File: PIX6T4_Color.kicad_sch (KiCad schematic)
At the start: 44 parts, among them J1 USB_C_Receptacle_USB2.0_16P, J2 Conn_01x18_Pin, J8 Conn_01x03, J9 SM03B-SRSS-TB, SW1 SW_MEC_5G, SW10 SW_MEC_5G, SW11 SW_MEC_5G, SW12 SW_MEC_5G, SW2 SW_MEC_5G, SW3 SW_MEC_5G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

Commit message: Rev. 2
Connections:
- net A: now also SW7.3 (B), SW7.4 (B), U3.7 (GPIO5); no longer SW8.3 (B), SW8.4 (B), U3.9 (GPIO7)
- net B: now also SW8.3 (B), SW8.4 (B), U3.9 (GPIO7); no longer SW7.3 (B), SW7.4 (B), U3.7 (GPIO5)
- net RGB63/RGB_OUT renamed RGB71/RGB_OUT
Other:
- added sheet RGB64 (RGB.kicad_sch)
- added sheet RGB65 (RGB.kicad_sch)
- added sheet RGB66 (RGB.kicad_sch)
- added sheet RGB67 (RGB.kicad_sch)
- added sheet RGB68 (RGB.kicad_sch)
- added sheet RGB69 (RGB.kicad_sch)
- added sheet RGB70 (RGB.kicad_sch)
- added sheet RGB71 (RGB.kicad_sch)
- moved on the sheet: J8

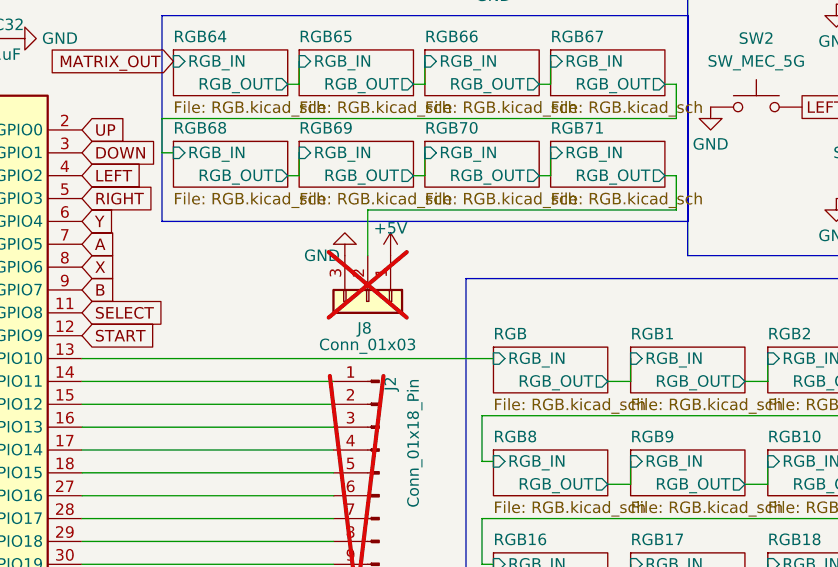
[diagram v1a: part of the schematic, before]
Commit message: Add power / invader logo light
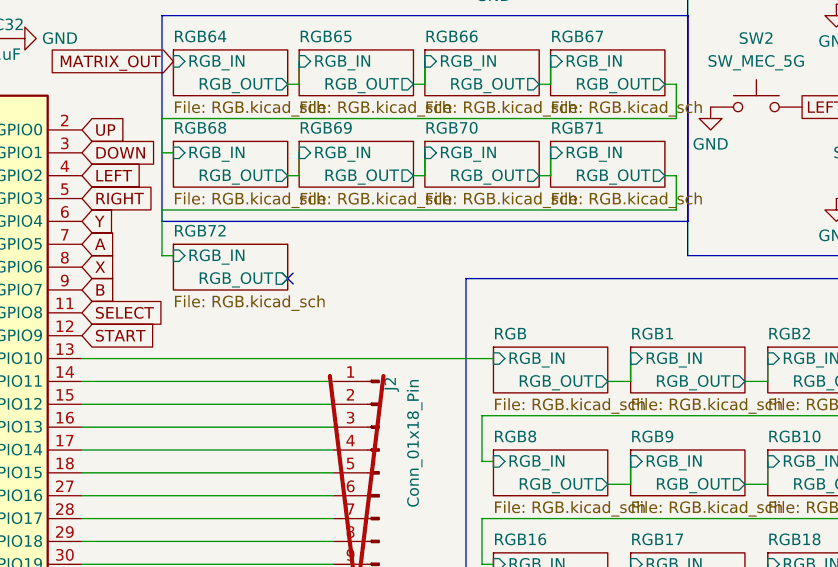
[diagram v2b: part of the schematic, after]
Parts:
- removed J8: Conn_01x03, Connector_JST:JST_SH_BM03B-SRSS-TB_1x03-1MP_P1.00mm_Vertical, symbol Connector_Generic:Conn_01x03
- SW11, SW12: footprint easyeda2kicad:SW-SMD_TS24CA -> easyeda2kicad:SW-SMD_2P-TS24CA
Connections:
- no-connect marks 2 -> 3
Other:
- added sheet RGB72 (RGB.kicad_sch)
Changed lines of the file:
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@@
 	)
 	(no_connect
+		(at 134.62 64.77)
+	)
+	(no_connect
 		(at 41.91 176.53)
 	)
@@
 	(wire
 		(pts
+			(xy 120.65 57.15) (xy 177.8 57.15)
+		)
+		(stroke
+			(width 0)
+			(type default)
+		)
+	)
+	(wire
+		(pts
 			(xy 120.65 50.8) (xy 121.92 50.8)
 		)
@@
 	(wire
 		(pts
-			(xy 177.8 57.15) (xy 143.51 57.15)
-		)
-		(stroke
-			(width 0)
-			(type default)
-		)
-	)
-	(wire
-		(pts
 			(xy 215.9 144.78) (xy 218.44 144.78)
 		)
@@
 	(wire
 		(pts
-			(xy 143.51 57.15) (xy 143.51 62.23)
-		)
-		(stroke
-			(width 0)
-			(type default)
-		)
-	)
-	(wire
-		(pts
 			(xy 52.705 125.73) (xy 52.705 127.635)
 		)
@@
 	(wire
 		(pts
+			(xy 120.65 57.15) (xy 120.65 62.23)
+		)
+		(stroke
+			(width 0)
+			(type default)
+		)
+	)
+	(wire
+		(pts
 			(xy 20.32 153.67) (xy 20.32 181.61)
 		)
@@
 	(wire
 		(pts
+			(xy 120.65 62.23) (xy 121.92 62.23)
+		)
+		(stroke
+			(width 0)
+			(type default)
+		)
+	)
+	(wire
+		(pts
 			(xy 278.13 110.49) (xy 278.13 114.3)
 		)
@@
 	)
 	(symbol
-		(lib_id "Connector_Generic:Conn_01x03")
-		(at 143.51 67.31 270)
-		(unit 1)
-		(exclude_from_sim no)
-		(in_bom yes)
-		(on_board yes)
-		(dnp yes)
-		(property "Reference" "J8"
-			(at 143.1544 70.3001 90)
-			(effects
-				(font
-					(size 1.27 1.27)
-				)
-			)
-		)
-		(property "Value" "Conn_01x03"
-			(at 143.51 72.136 90)
-			(effects
-				(font
-					(size 1.27 1.27)
-				)
-			)
-		)
-		(property "Footprint" "Connector_JST:JST_SH_BM03B-SRSS-TB_1x03-1MP_P1.00mm_Vertical"
-			(at 143.51 67.31 0)
-			(effects
-				(font
-					(size 1.27 1.27)
-				)
-				(hide yes)
-			)
-		)
-		(property "Datasheet" "~"
-			(at 143.51 67.31 0)
-			(effects
-				(font
-					(size 1.27 1.27)
-				)
-				(hide yes)
-			)
-		)
-		(property "Description" "Generic connector, single row, 01x03, script generated (kicad-library-utils/schlib/autogen/connector/)"
-			(at 143.51 67.31 0)
-			(effects
-				(font
-					(size 1.27 1.27)
-				)
-				(hide yes)
-			)
-		)
-		(property "JLCPCB Part #" "C160389"
-			(at 143.51 67.31 0)
-			(effects
-				(font
-					(size 1.27 1.27)
-				)
-				(hide yes)
-			)
-		)
-		(property "JLCPCB Rotation Offset" "180"
-			(at 143.51 67.31 0)
-			(effects
-				(font
-					(size 1.27 1.27)
-				)
-				(hide yes)
-			)
-		)
-		(pin "3"
-		)
-		(pin "2"
-		)
-		(pin "1"
-		)
-		(instances
-			(project "PIX6T4_Color"
-				(path "/279815f6-a512-43c8-bc8d-a03c0593ab83"
-					(reference "J8")
-					(unit 1)
-				)
-			)
-		)
-	)
-	(symbol
 		(lib_id "Device:C")
 		(at 104.14 165.1 0)
@@
 	)
 	(symbol
+		(lib_name "SW_MEC_5G_1")
 		(lib_id "Switch:SW_MEC_5G")
 		(at 49.53 88.9 0)
@@
 			)
 		)
-		(property "Footprint" "easyeda2kicad:SW-SMD_TS24CA"
+		(property "Footprint" "easyeda2kicad:SW-SMD_2P-TS24CA"
 			(at 49.53 83.82 0)
 			(effects
@@
 	)
 	(symbol
-		(lib_id "power:GND")
-		(at 140.97 62.23 180)
-		(unit 1)
-		(exclude_from_sim no)
-		(in_bom yes)
-		(on_board yes)
-		(dnp no)
-		(property "Reference" "#PWR0174"
-			(at 140.97 55.88 0)
-			(effects
-				(font
-					(size 1.27 1.27)
-				)
-				(hide yes)
-			)
-		)
-		(property "Value" "GND"
-			(at 138.43 62.23 0)
-			(effects
-				(font
-					(size 1.27 1.27)
-				)
-			)
-		)
-		(property "Footprint" ""
-			(at 140.97 62.23 0)
-			(effects
-				(font
-					(size 1.27 1.27)
-				)
-				(hide yes)
-			)
-		)
-		(property "Datasheet" ""
-			(at 140.97 62.23 0)
-			(effects
-				(font
-					(size 1.27 1.27)
-				)
-				(hide yes)
-			)
-		)
-		(property "Description" ""
-			(at 140.97 62.23 0)
-			(effects
-				(font
-					(size 1.27 1.27)
-				)
-				(hide yes)
-			)
-		)
-		(pin "1"
-		)
-		(instances
-			(project "PIX6T4_Color"
-				(path "/279815f6-a512-43c8-bc8d-a03c0593ab83"
-					(reference "#PWR0174")
-					(unit 1)
-				)
-			)
-		)
-	)
-	(symbol
 		(lib_id "Switch:SW_MEC_5G")
 		(at 55.88 48.26 0)
@@
 			)
 		)
-		(property "Footprint" "easyeda2kicad:SW-SMD_TS24CA"
+		(property "Footprint" "easyeda2kicad:SW-SMD_2P-TS24CA"
 			(at 55.88 43.18 0)
 			(effects
@@
 	)
 	(symbol
-		(lib_id "power:+3V3")
-		(at 146.05 62.23 0)
-		(unit 1)
-		(exclude_from_sim no)
-		(in_bom yes)
-		(on_board yes)
-		(dnp no)
-		(property "Reference" "#PWR0175"
-			(at 146.05 66.04 0)
-			(effects
-				(font
-					(size 1.27 1.27)
-				)
-				(hide yes)
-			)
-		)
-		(property "Value" "+5V"
-			(at 146.05 59.182 0)
-			(effects
-				(font
-					(size 1.27 1.27)
-				)
-			)
-		)
-		(property "Footprint" ""
-			(at 146.05 62.23 0)
-			(effects
-				(font
-					(size 1.27 1.27)
-				)
-				(hide yes)
-			)
-		)
-		(property "Datasheet" ""
-			(at 146.05 62.23 0)
-			(effects
-				(font
-					(size 1.27 1.27)
-				)
-				(hide yes)
-			)
-		)
-		(property "Description" ""
-			(at 146.05 62.23 0)
-			(effects
-				(font
-					(size 1.27 1.27)
-				)
-				(hide yes)
-			)
-		)
-		(pin "1"
-		)
-		(instances
-			(project "PIX6T4_Color"
-				(path "/279815f6-a512-43c8-bc8d-a03c0593ab83"
-					(reference "#PWR0175")
-					(unit 1)
-				)
-			)
-		)
-	)
-	(symbol
 		(lib_id "power:GND")
 		(at 119.38 127 0)
@@
 				)
 			)
+		)
+	)
+	(sheet
+		(at 121.92 60.96)
+		(size 12.7 5.08)
+		(exclude_from_sim no)
+		(in_bom yes)
+		(on_board yes)
+		(dnp no)
+		(fields_autoplaced yes)
+		(stroke
+			(width 0.1524)
+			(type solid)
+		)
+		(fill
+			(color 0 0 0 0.0000)
+		)
+		(property "Sheetname" "RGB72"
+			(at 121.92 60.2484 0)
+			(effects
+				(font
+					(size 1.27 1.27)
+				)
+				(justify left bottom)
+			)
+		)
+		(property "Sheetfile" "RGB.kicad_sch"
+			(at 121.92 66.6246 0)
+			(effects
+				(font
+					(size 1.27 1.27)
+				)
+				(justify left top)
+			)
+		)
+		(pin "RGB_IN" input
+			(at 121.92 62.23 180)
+			(effects
+				(font
+					(size 1.27 1.27)
+				)
+				(justify left)
+			)
+		)
+		(pin "RGB_OUT" output
+			(at 134.62 64.77 0)
+			(effects
+				(font
+					(size 1.27 1.27)
+				)
+				(justify right)
+			)
+		)
+		(instances
+			(project "PIX6T4_Color"
+				(path "/279815f6-a512-43c8-bc8d-a03c0593ab83"
+					(page "74")
+				)
+			)
